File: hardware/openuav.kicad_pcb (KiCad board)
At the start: 4 copper layers, 36 x 36 mm, 95 parts, among them J1 Conn_01x01, J10 Conn_01x01, J11 Conn_01x01, J12 Conn_01x01, J13 Conn_01x01, J14 Conn_01x01, J15 Conn_01x01, J16 Conn_01x01, J17 Conn_01x01, J18 Conn_01x01, J19 Conn_01x01, J2 Conn_01x01, J20 Conn_01x01, J21 Conn_01x01, J22 Conn_01x01, J23 Conn_01x01, J24 Conn_01x01, J25 Conn_01x01, J3 Conn_01x01, J4 Conn_01x01, J5 Conn_01x01, J6 Conn_01x01, J7 Conn_01x01, J8 Conn_01x01, J9 Conn_01x01, J99 USB_C_Receptacle_USB2.0, SW1 SW_Push, U1 STM32G431CBUx, U2 LPS22HH, U3 LSM6DSR, U6 W25N01GVZEIG, U7 TLV75733PDBV, U8 TLV75733PDBV

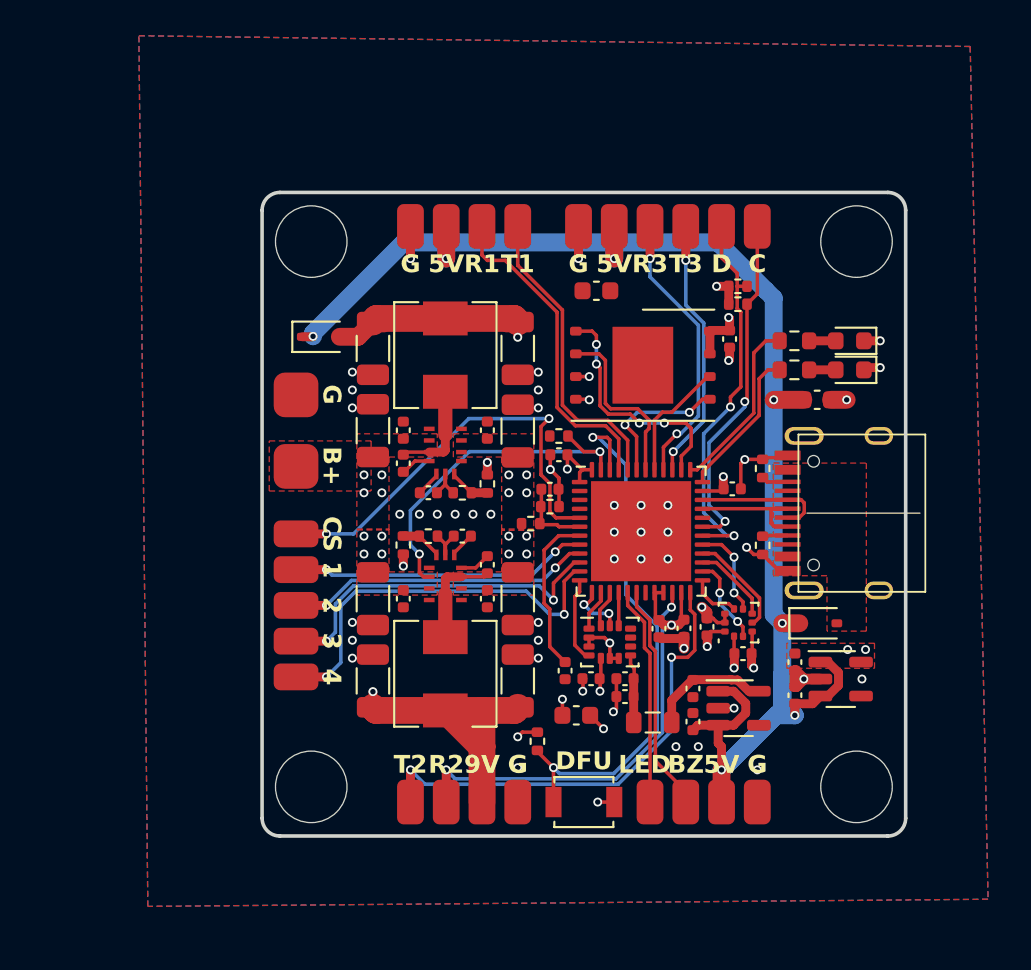
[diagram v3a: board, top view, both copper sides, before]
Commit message: Revert v1 hardware, remove unused code for v2 hardware
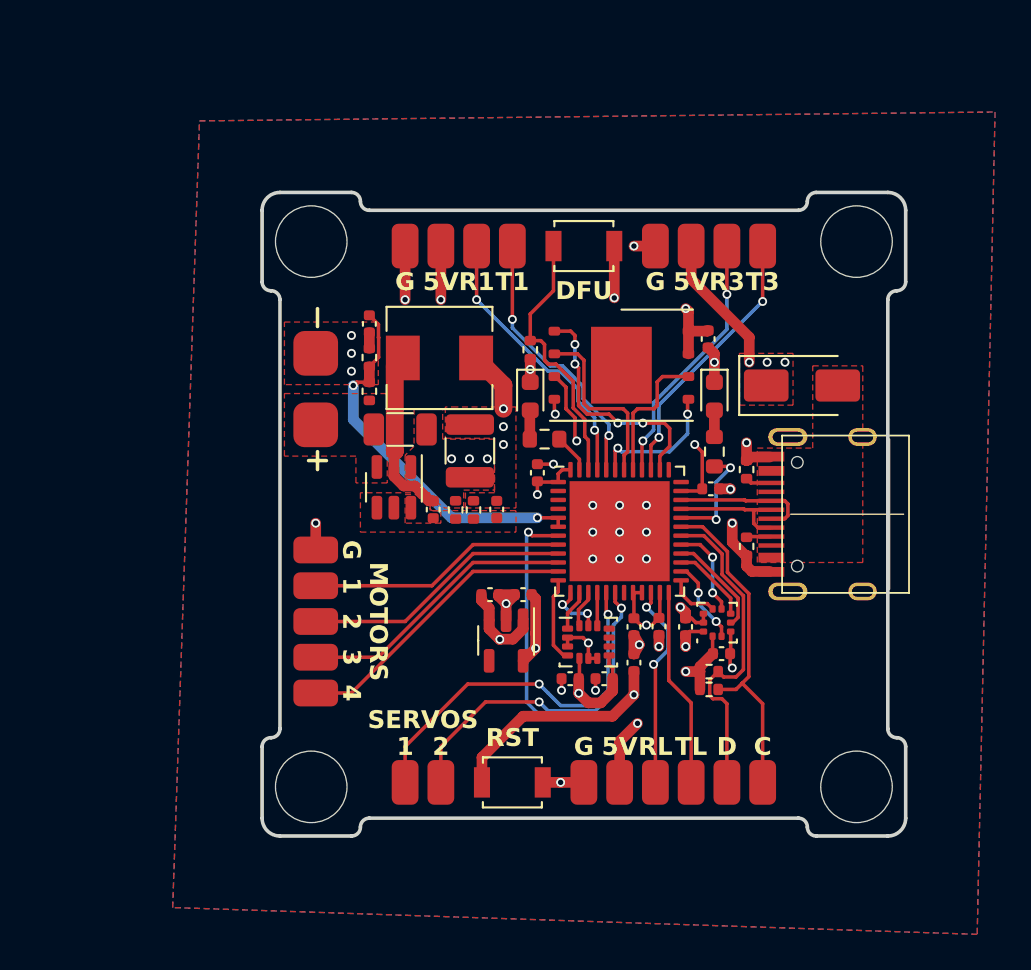
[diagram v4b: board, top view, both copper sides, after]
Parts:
- removed C17, C18, C20, C23: 10u, Capacitor_SMD:C_1206_3216Metric
- removed C19, C21, C22, C27, C8: 100n, Capacitor_SMD:C_0402_1005Metric
- removed C26, C30, C31, C32: 1u, Capacitor_SMD:C_0402_1005Metric
- removed C28, C29: 22u, Capacitor_SMD:C_1206_3216Metric
- removed C33, C34, C35: 10u, Capacitor_SMD:C_0603_1608Metric
- removed D4: PMEG2020AEA, Diode_SMD:D_SOD-323
- removed FB1: FerriteBead, Inductor_SMD:L_0805_2012Metric
- removed J15, J16: Conn_01x01, footprints:largepad
- removed J17, J18: Conn_01x01, footprints:smallpad
- removed L2: 10u, Inductor_SMD:L_Sunlord_MWSA0503S
- removed R13: 10k, Resistor_SMD:R_0402_1005Metric
- removed R14: 22k, Resistor_SMD:R_0402_1005Metric
- removed R15: 2.44k, Resistor_SMD:R_0402_1005Metric
- removed U5: ~, footprints:RNX0012B
- removed U8: TLV75733PDBV, Package_TO_SOT_SMD:SOT-23-5
- added J30: Conn_01x01, footprints:largepad, F.Cu at (133.0, 63.0)
- added J31: Conn_01x01, footprints:largepad, F.Cu at (133.0, 59.0)
- added SW2: SW_Push, Button_Switch_SMD:SW_SPST_B3U-1000P, F.Cu at (144.0, 83.0)
- C10: value 22u -> 68p; footprint Capacitor_SMD:C_1206_3216Metric -> Capacitor_SMD:C_0402_1005Metric
- C15: value 22u -> 47u; footprint Capacitor_SMD:C_1206_3216Metric -> Capacitor_SMD:C_1210_3225Metric
- C2: value 1u -> 10u; footprint Capacitor_SMD:C_0402_1005Metric -> Capacitor_SMD:C_1206_3216Metric
- D1: value PMEG2020AEA -> SS34; footprint Diode_SMD:D_SOD-323 -> Diode_SMD:D_SMA
- R3: value 2.44k -> 100k
- R4: value 22k -> 13.3k
- U4: value ~ -> TPS54302; footprint footprints:RNX0012B -> Package_TO_SOT_SMD:SOT-23-6
- moved J8 36.8 mm to (158.0, 53.0)
- moved J7 34.8 mm to (156.0, 53.0)
- moved J5 31.6 mm to (152.0, 53.0), turned to 90 degrees
- moved J6 31.1 mm to (154.0, 53.0), turned to 90 degrees
- moved J10 31.1 mm to (150.0, 83.0)
- moved J11 31.1 mm to (152.0, 83.0)
- moved J12 31.1 mm to (154.0, 83.0)
- moved J19 31.1 mm to (156.0, 83.0)
- moved J20 31.1 mm to (158.0, 83.0)
- moved J9 31.1 mm to (148.0, 83.0)
- moved SW1 31.1 mm to (148.0, 53.0)
- moved R8 21.9 mm to (145.0, 58.8), turned to -90 degrees
- moved R10 21.6 mm to (155.0, 77.8)
- moved R9 21.6 mm to (155.0, 76.8)
- moved U7 18.8 mm to (143.7, 75.1), turned to -90 degrees
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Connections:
- C10 pad 1: +9V -> Net-(U4-FB)
- C10 pad 2: GND -> +5V
- C15 pad 1: +9V -> +5V
- C2 pad 1: Net-(U4-VCC) -> +BATT
- C3 pad 1: VDDA -> +3V3
- C9 pad 1: Net-(U4-NC) -> Net-(U4-BOOT)
- C9 pad 2: Net-(U4-BOOT) -> Net-(U4-SW)
- J11 pad 1: UART_3_RX -> UART_4_RX
- J12 pad 1: UART_3_TX -> UART_4_TX
- J7 pad 1: UART_4_RX -> UART_3_RX
- J8 pad 1: UART_4_TX -> UART_3_TX
- L1 pad 1: Net-(U4-NC) -> Net-(U4-SW)
- L1 pad 2: +9V -> +5V
- R3 pad 1: Net-(U4-FB) -> +5V
- R3 pad 2: GND -> Net-(U4-FB)
- R4 pad 1: +9V -> Net-(U4-FB)
- R4 pad 2: Net-(U4-FB) -> GND
- U1 pad 32: unconnected-(U1-PA10-Pad32) -> LED2
- U1 pad 36: LED2 -> SWDIO
- U1 pad 37: LED1 -> SWCLK
- U1 pad 47: 9VEN -> LED1
- U1 pad 5: CURRENT -> VOLTAGE
- U3 pad 8: VDDA -> +3V3
- U4 pad 2: +BATT -> Net-(U4-SW)
- U4 pad 3: Net-(U4-NC) -> +BATT
- U4 pad 4: Net-(U4-BOOT) -> Net-(U4-FB)
- U4 pad 5: Net-(U4-VCC) -> unconnected-(U4-EN-Pad5)
- U4 pad 6: GND -> Net-(U4-BOOT)
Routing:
- net +5V: track 89.5 -> 23.0 mm, vias 7 -> 9
- net +9V: track 25.5 -> 0.00 mm, vias 2 -> 0
- net CURRENT: track 24.2 -> 0.00 mm, vias 2 -> 0
- net NRST: track 9.07 -> 30.8 mm, vias 0 -> 2
- net Net-(D4-A): track 19.7 -> 0.00 mm, vias 2 -> 0
- net 9VEN: track 19.5 -> 0.00 mm, vias 2 -> 0
- net VOLTAGE: track 4.26 -> 21.3 mm, vias 0 -> 2
- net +3V3: track 23.0 -> 39.2 mm, vias 13 -> 10
- net BOOT0: track 30.8 -> 15.0 mm, vias 2 -> 0
- net UART_4_TX: track 26.9 -> 11.1 mm, vias 2 -> 0
- net UART_4_RX: track 23.2 -> 11.6 mm
- net PWM_5: track 12.2 -> 21.2 mm, vias 0 -> 2
- net Net-(U4-SW): track 0.00 -> 8.70 mm
- net LED1: track 9.96 -> 2.18 mm
- net Net-(U8-OUT): track 6.86 -> 0.00 mm
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- added copper zone on B.Cu, net (none)
- added copper zone on F.Cu, net (none)
- added copper zone on In1.Cu, net +3V3
- added copper zone on F.Cu, net +5V
- added copper zone on In1.Cu, net +5V
- added copper zone on In2.Cu, net GND
- added copper zone on F.Cu, net Net-(U4-BOOT)
- added copper zone on F.Cu, net Net-(U4-FB)
- removed copper zone on F.Cu, net +3V3
- removed copper zone on In2.Cu, net +3V3
- removed copper zone on In2.Cu, net +BATT
- removed copper zone on B.Cu, net GND
- removed copper zone on In1.Cu, net GND
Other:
- outline, holes or cut-outs redrawn
- board text added: "MOTORS"
- board text added: "OPENUAV v0.2"
- board text added: "RL"
- board text added: "RST"
- board text added: "SERVOS"
- board text added: "TL"
- board text removed: "9V"
- board text removed: "B+"
- board text removed: "BZ"
- board text removed: "CS"
- board text removed: "LED"
- board text removed: "OPENUAV v0.3"
- board text removed: "R2"
- board text removed: "T2"

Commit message: Increase board size
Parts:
- moved J99 0.90 mm to (164.5, 68.0)
- moved R1 0.90 mm to (158.0, 65.5)
- moved R2 0.90 mm to (158.0, 69.8)
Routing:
- net USB_DP: track 7.72 -> 8.59 mm
- net USB_DM: track 6.92 -> 7.80 mm
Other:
- outline, holes or cut-outs redrawn
- board text added: "GPIO"
- board text removed: "SERVOS"

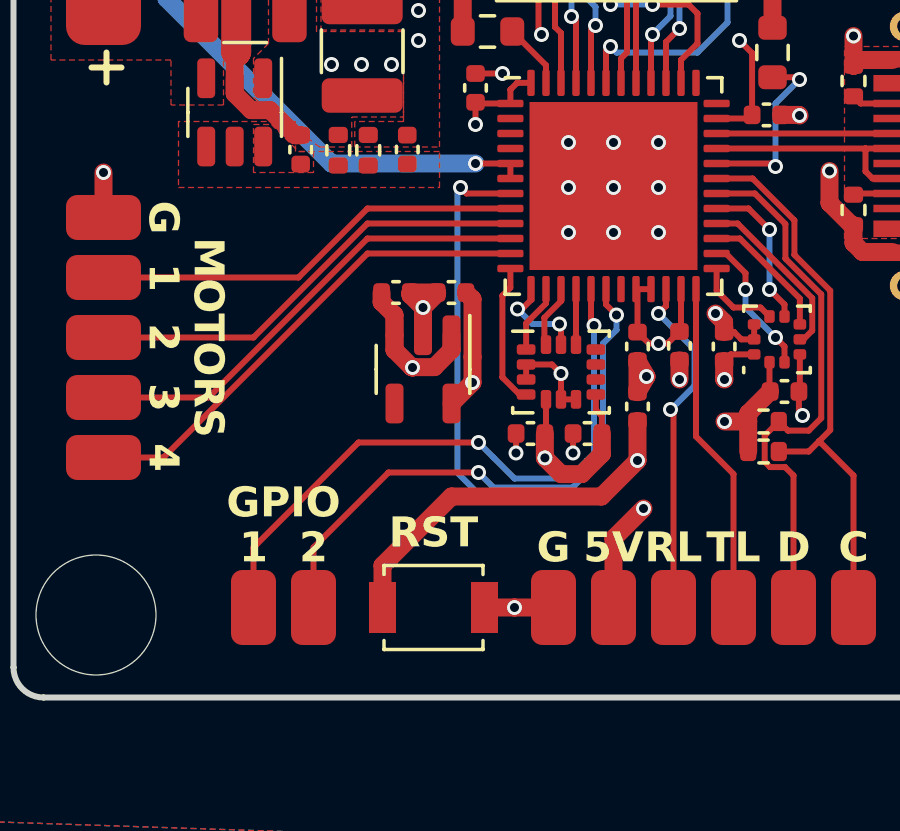
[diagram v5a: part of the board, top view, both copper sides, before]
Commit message: Remove reset button
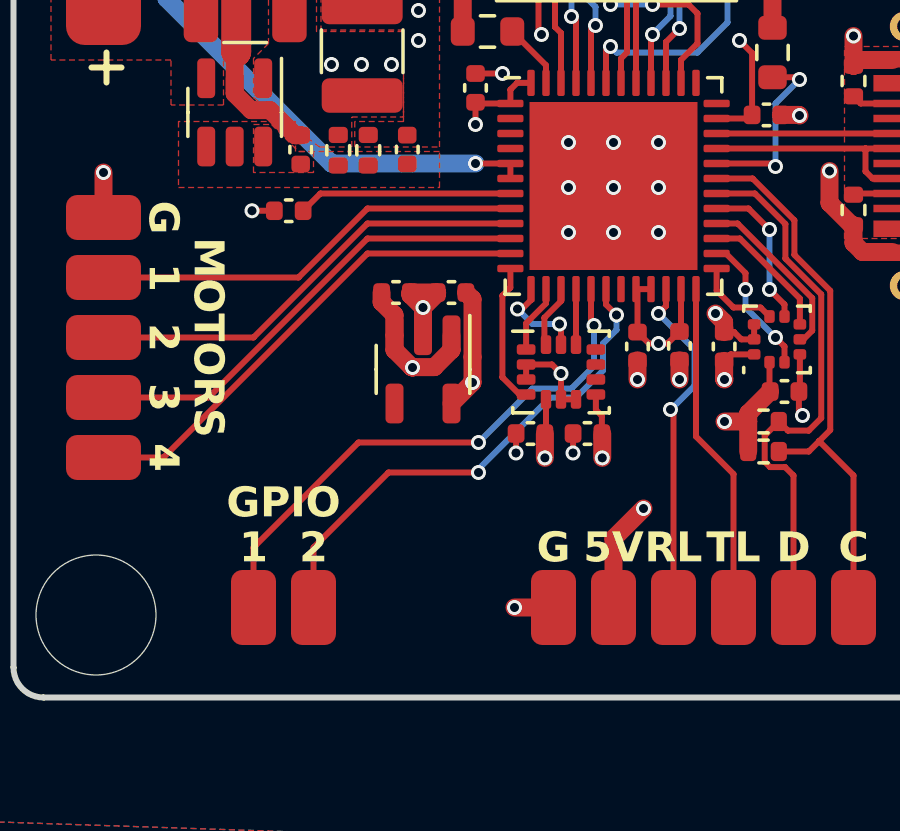
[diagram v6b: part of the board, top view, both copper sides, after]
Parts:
- removed SW2: SW_Push, Button_Switch_SMD:SW_SPST_B3U-1000P
- moved C1 13.3 mm to (139.2, 69.8), turned to 0 degrees
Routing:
- net NRST: track 30.8 -> 7.15 mm, vias 2 -> 0
- net PWM_5: track 21.2 -> 18.5 mm
- net +3V3: track 39.2 -> 36.9 mm, vias 10 -> 11
- net PWM_6: track 19.2 -> 17.2 mm
- net GND: track 36.4 -> 34.6 mm, vias 34 -> 35
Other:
- board text removed: "RST"

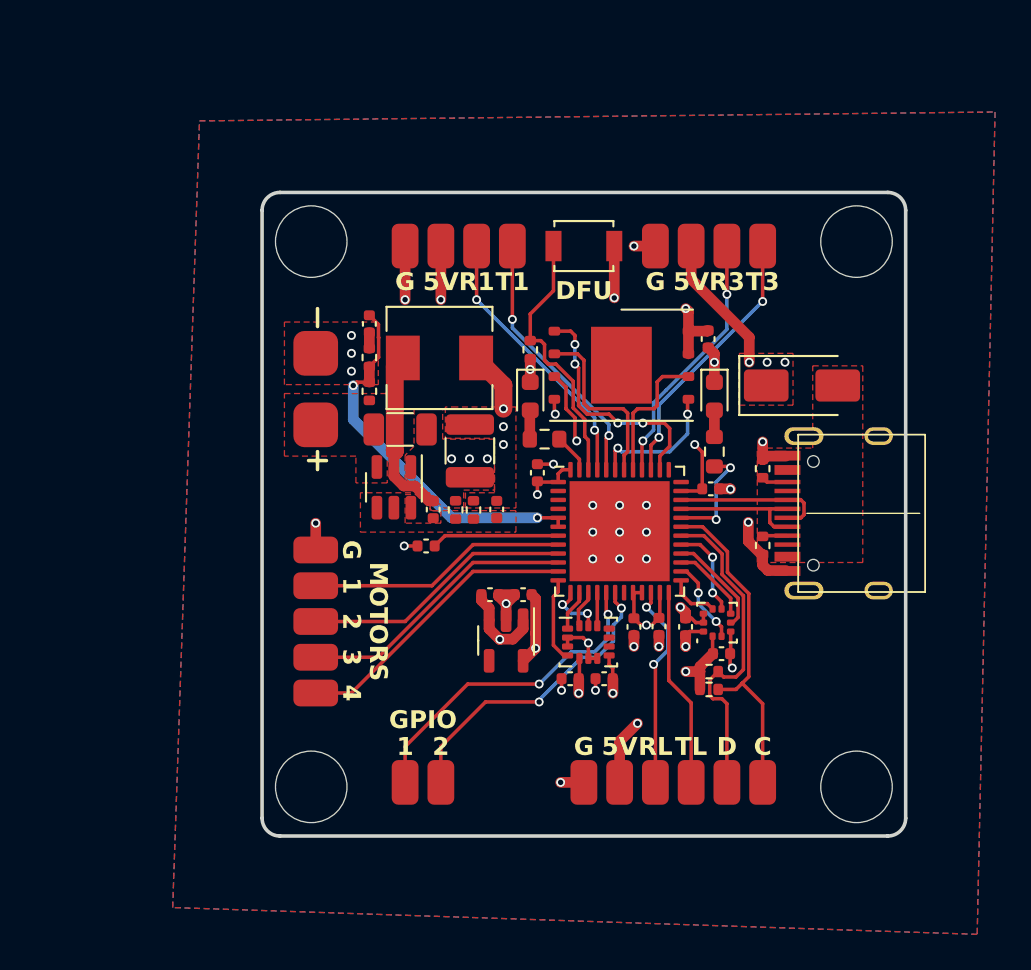
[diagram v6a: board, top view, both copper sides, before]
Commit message: Move pads to edge of board
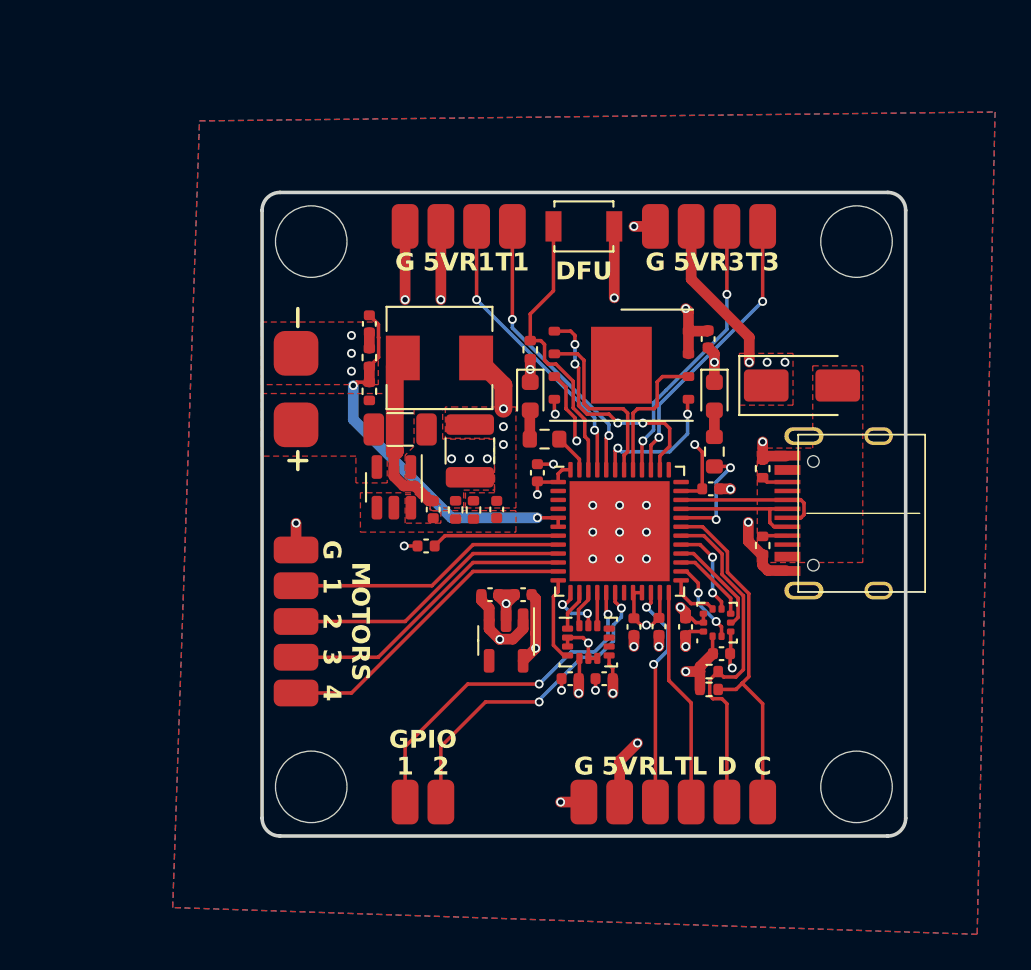
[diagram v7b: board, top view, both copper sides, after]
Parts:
- moved J1 1.10 mm to (138.0, 51.9)
- moved J2 1.10 mm to (140.0, 51.9)
- moved J3 1.10 mm to (142.0, 51.9)
- moved J4 1.10 mm to (144.0, 51.9)
- moved J5 1.10 mm to (152.0, 51.9)
- moved J6 1.10 mm to (154.0, 51.9)
- moved J7 1.10 mm to (156.0, 51.9)
- moved J8 1.10 mm to (158.0, 51.9)
- moved SW1 1.10 mm to (148.0, 51.9)
- moved J10 1.10 mm to (150.0, 84.1)
- moved J11 1.10 mm to (152.0, 84.1)
- moved J12 1.10 mm to (154.0, 84.1)
- moved J13 1.10 mm to (138.0, 84.1)
- moved J14 1.10 mm to (140.0, 84.1)
- moved J19 1.10 mm to (156.0, 84.1)
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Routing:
- net +5V: track 23.0 -> 25.2 mm
- net BOOT0: track 15.0 -> 16.1 mm
- net UART_3_TX: track 15.1 -> 16.2 mm
- net UART_3_RX: track 14.5 -> 15.6 mm
- net UART_1_TX: track 14.8 -> 15.9 mm
- net UART_1_RX: track 15.3 -> 16.4 mm
- net +3V3: track 36.9 -> 38.0 mm
- net UART_4_TX: track 11.1 -> 12.2 mm
- net UART_4_RX: track 11.6 -> 12.7 mm
- net PWM_6: track 17.2 -> 18.3 mm
- net PWM_5: track 18.5 -> 19.6 mm
- net PWM_4: track 16.4 -> 17.5 mm
- net PWM_3: track 15.8 -> 16.9 mm
- net PWM_2: track 15.1 -> 16.2 mm
- net PWM_1: track 14.5 -> 15.6 mm
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
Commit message: Move DFU button
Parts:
- removed J21: Conn_01x01, footprints:smallpad
- moved SW1 29.5 mm to (131.9, 76.6), turned to 90 degrees
- moved R8 15.5 mm to (145.6, 74.3)
- moved J22 5.40 mm to (131.9, 66.6)
- moved J23 5.40 mm to (131.9, 68.6)
- moved J24 5.40 mm to (131.9, 70.6)
- moved J25 5.40 mm to (131.9, 72.6)
- moved C1 4.53 mm to (143.7, 69.6)
- moved C24 0.83 mm to (143.8, 72.8)
- moved C25 0.83 mm to (142.0, 72.8)
- moved U7 0.83 mm to (142.9, 75.4)
- moved C7 0.10 mm to (150.9, 74.3)
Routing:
- net +3V3: track 38.0 -> 52.8 mm
- net BOOT0: track 16.1 -> 26.4 mm, vias 0 -> 2
- net NRST: track 7.15 -> 2.55 mm
- net PWM_5: track 19.6 -> 22.1 mm, vias 2 -> 0
- net GND: track 35.7 -> 33.2 mm
- net PWM_4: track 17.5 -> 15.2 mm
- net PWM_6: track 18.3 -> 20.3 mm, vias 2 -> 0
- net PWM_3: track 16.9 -> 14.9 mm
- net PWM_1: track 15.6 -> 17.6 mm
- net +5V: track 25.2 -> 23.9 mm
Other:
- board text removed: "MOTORS"
